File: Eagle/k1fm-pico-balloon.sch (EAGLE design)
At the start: 40 parts, among them J1 I2C, J2 ICSP, J3 SERIAL, J4 POWER, Q1 ASTX-H11-25.000MHZ-T, Q2 DMP2305U, Q3 DMP2305U, U1 ATMEGA328, U2 Si5351A-B-GT, U3 MCP1754X-XXXXX/C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

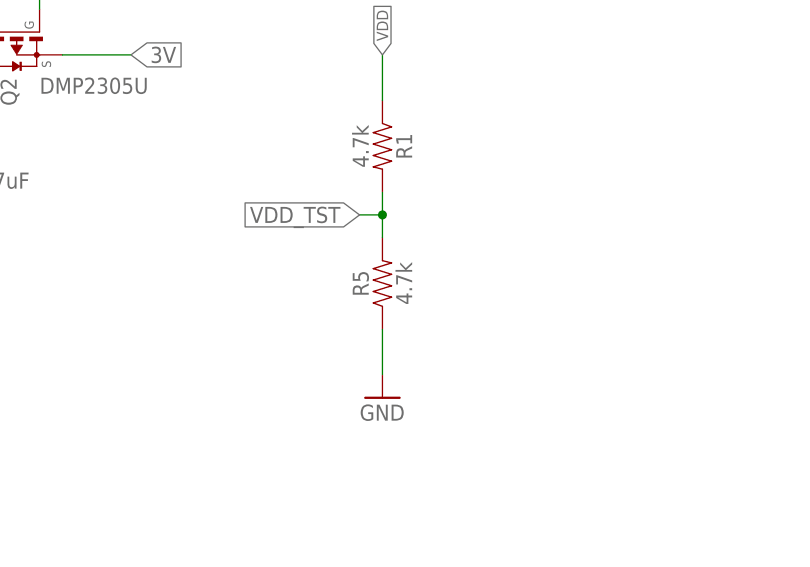
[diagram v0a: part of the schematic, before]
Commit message: Fixed R1-R5 voltage divider, fixed PCB warnings
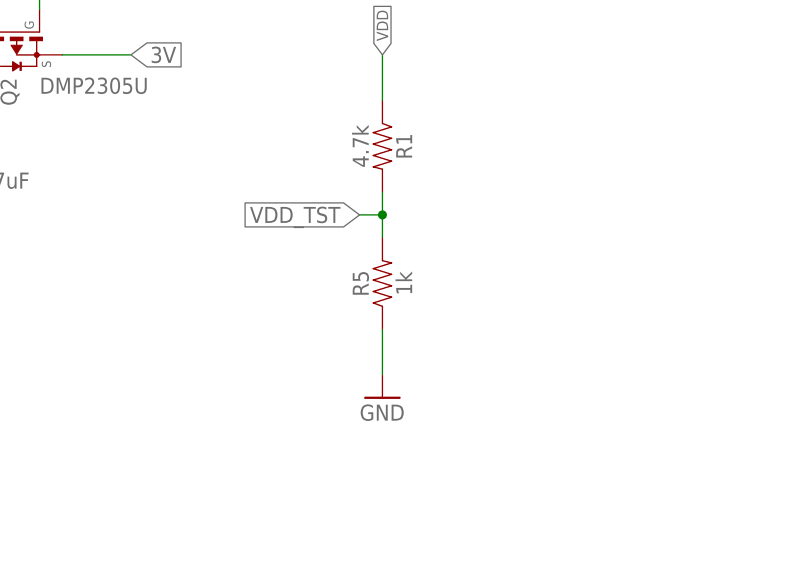
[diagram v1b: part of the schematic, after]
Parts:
- R5: value 4.7k -> 1k
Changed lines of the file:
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@@
 <part name="GND21" library="SparkFun-Aesthetics" library_urn="urn:adsk.eagle:library:507" deviceset="GND" device=""/>
 <part name="R1" library="SparkFun-Resistors" library_urn="urn:adsk.eagle:library:532" deviceset="10KOHM" device="-0603-1/10W-1%" package3d_urn="urn:adsk.eagle:package:39650/1" value="4.7k"/>
-<part name="R5" library="SparkFun-Resistors" library_urn="urn:adsk.eagle:library:532" deviceset="10KOHM" device="-0603-1/10W-1%" package3d_urn="urn:adsk.eagle:package:39650/1" value="4.7k"/>
+<part name="R5" library="SparkFun-Resistors" library_urn="urn:adsk.eagle:library:532" deviceset="10KOHM" device="-0603-1/10W-1%" package3d_urn="urn:adsk.eagle:package:39650/1" value="1k"/>
 <part name="GND22" library="SparkFun" deviceset="GND" device=""/>
 <part name="U4" library="TMP36" deviceset="TMP36" device=""/>
